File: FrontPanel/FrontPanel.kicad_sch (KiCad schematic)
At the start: 75 parts, among them J1 CPU, J2 Backplane, J3 Conn_01x05_Male, J4 Conn_01x05_Female, SW1 SELECT, SW2 OPSYS, SW3 R/F, U1 74LS38, U2 74LS38, U3 74LS123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

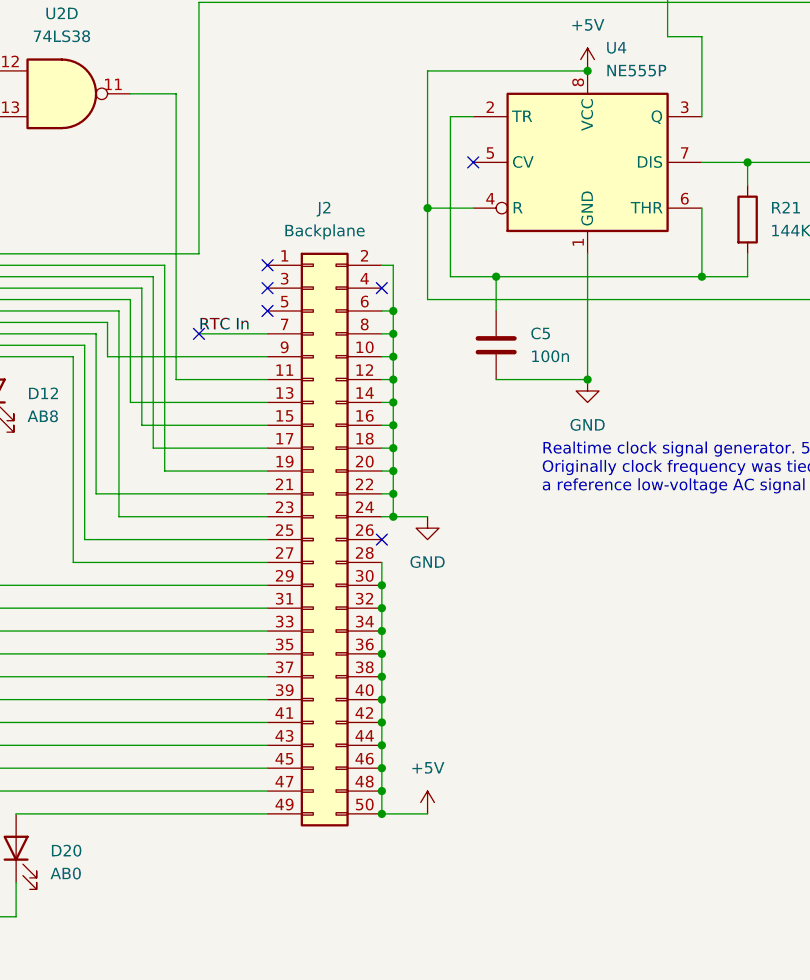
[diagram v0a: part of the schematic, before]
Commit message: FrontPanel: Fixed J2 bottom pinout
Fix swapped 5V and GND, verified with the photo
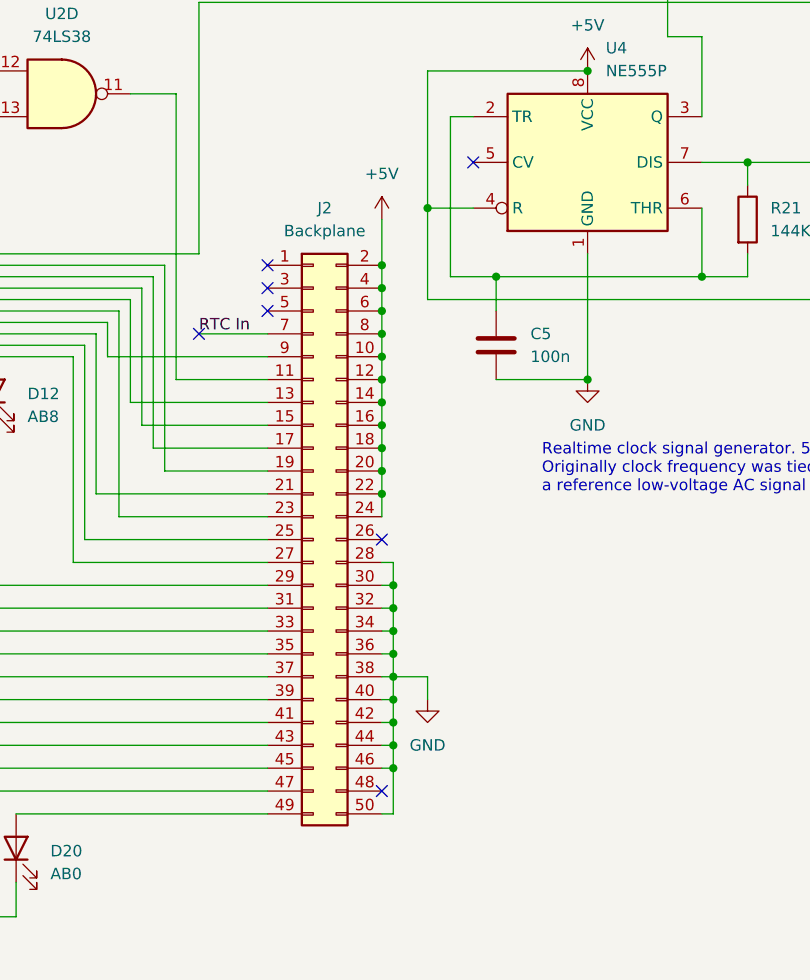
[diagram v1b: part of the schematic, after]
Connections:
- net +5V: now also J2.10 (Pin_10), J2.12 (Pin_12), J2.14 (Pin_14), J2.16 (Pin_16), J2.18 (Pin_18), J2.2 (Pin_2), J2.20 (Pin_20), J2.22 (Pin_22), J2.24 (Pin_24), J2.4 (Pin_4), J2.6 (Pin_6), J2.8 (Pin_8); no longer J2.28 (Pin_28), J2.30 (Pin_30), J2.32 (Pin_32), J2.34 (Pin_34), J2.36 (Pin_36), J2.38 (Pin_38), J2.40 (Pin_40), J2.42 (Pin_42), J2.44 (Pin_44), J2.46 (Pin_46), J2.48 (Pin_48), J2.50 (Pin_50)
- net GND: now also J2.28 (Pin_28), J2.30 (Pin_30), J2.32 (Pin_32), J2.34 (Pin_34), J2.36 (Pin_36), J2.38 (Pin_38), J2.40 (Pin_40), J2.42 (Pin_42), J2.44 (Pin_44), J2.46 (Pin_46), J2.50 (Pin_50); no longer J2.10 (Pin_10), J2.12 (Pin_12), J2.14 (Pin_14), J2.16 (Pin_16), J2.18 (Pin_18), J2.2 (Pin_2), J2.20 (Pin_20), J2.22 (Pin_22), J2.24 (Pin_24), J2.6 (Pin_6), J2.8 (Pin_8)

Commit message: FrontPanel: Complete
Add potentiometer to adjust clock frequency and better connector for buttons.
Complete the layout.
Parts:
- added RV1: 50K, Potentiometer_THT:Potentiometer_Bourns_3299Y_Vertical, symbol Device:R_Potentiometer
- D30, D31, D32, D33, D34, D35: value D -> 1N4148
- J3: value Conn_01x05_Male -> MPW-Y; footprint Connector_PinHeader_2.54mm:PinHeader_1x05_P2.54mm_Vertical -> Connector_Phoenix_MSTB:PhoenixContact_MSTBVA_2,5_5-G-5,08_1x05_P5.08mm_Vertical
- R21: value 144K -> 100K
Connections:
- net at C5.1, U4.2 (TR), U4.6 (THR): now also R21.1; no longer R21.2
- net at R22.1, U4.7 (DIS): now also RV1.1, RV1.2; no longer R21.1
- new net: R21.2, RV1.3
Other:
- note added: "Adjust to get 50 or 60 Hz"
- moved on the sheet: R21, R22
